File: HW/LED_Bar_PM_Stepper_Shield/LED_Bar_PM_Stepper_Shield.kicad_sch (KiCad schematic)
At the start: 14 parts, among them J5 1x6 2.54mm female, pin2 filled, J6 1x6 2.54mm female, pin2 filled, J7 Extension of Ard Nano, filled, J8 Extension of Ard Nano, filled

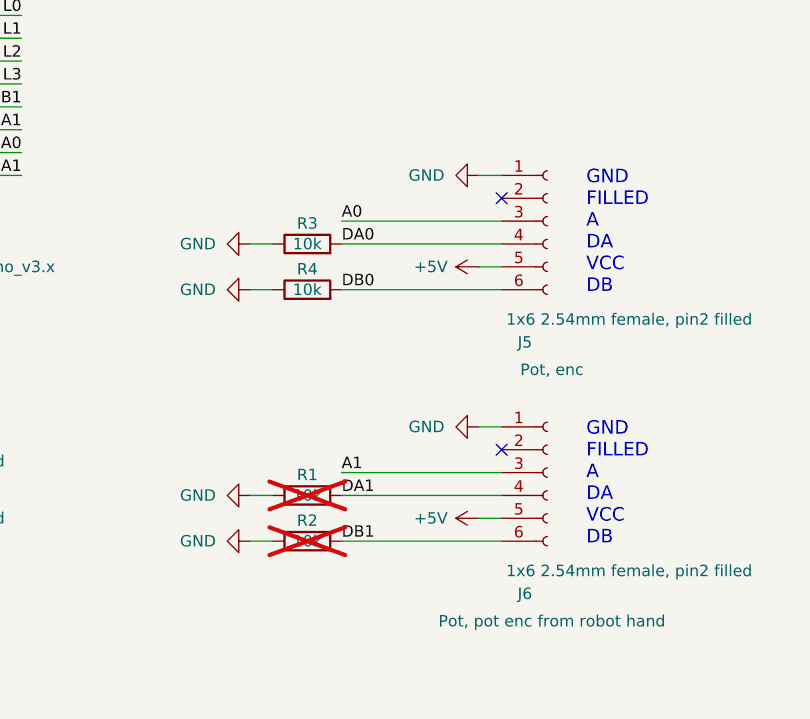
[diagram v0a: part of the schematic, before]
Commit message: Swapped GND and 5V so I can use internal Pull-up.
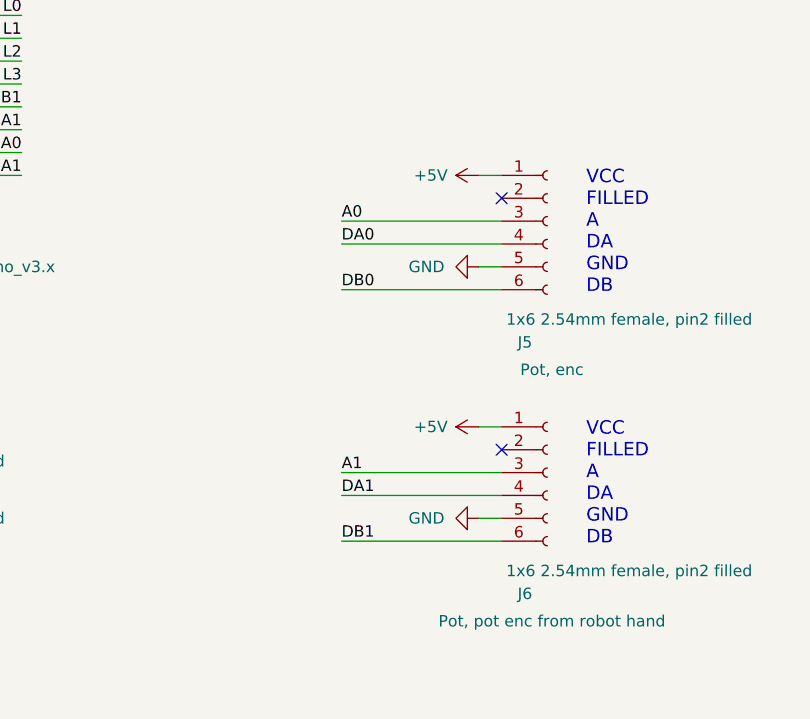
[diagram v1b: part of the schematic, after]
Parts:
- removed R1, R2, R3, R4: 10k, For_Rasterboard:R_Axial_DIN0207_L6.3mm_D2.5mm_Pinf_Horizontal, symbol Device:R
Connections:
- net +5V: now also J5.1 (Pin_1), J6.1 (Pin_1); no longer J5.5 (Pin_5), J6.5 (Pin_5)
- net GND: now also J5.5 (Pin_5), J6.5 (Pin_5); no longer J5.1 (Pin_1), J6.1 (Pin_1)
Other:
- note added: "VCC FILLED A DA GND DB"
- note removed: "GND FILLED A DA VCC DB"

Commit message: All done.
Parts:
- added D3, D5: 1N5400, Diode_THT:D_DO-201AD_P5.08mm_Vertical_AnodeUp, symbol Diode:1N5400
- added D4: 3mm yellow, For_Rasterboard:LED_D3.0mm_Pinf, symbol Device:LED
- added J10: 2-pin KK254, Connector_Molex:Molex_KK-254_AE-6410-02A_1x02_P2.54mm_Vertical, symbol Connector_Generic:Conn_01x02
- added J9: Barrel_Jack_Switch, Connector_BarrelJack:BarrelJack_Horizontal, symbol Connector:Barrel_Jack_Switch
- added Q1: IRLZ34N, Package_TO_SOT_THT:TO-220-3_Vertical, symbol Transistor_FET:IRLZ34N
- added R1: 470, For_Rasterboard:R_Axial_DIN0207_L6.3mm_D2.5mm_P7.62mm_Horizontal, symbol Device:R
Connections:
- net +5V: now also D3.1 (K), D4.2 (A), D5.1 (K), J10.1 (Pin_1), J9.1
- net GND: now also D5.2 (A), J9.2, J9.3, Q1.3 (S)
- net b0/B2 renamed S2
- net b0/B3 renamed S3
- net S3: now also Q1.1 (G)
- new net: D3.2 (A), J10.2 (Pin_2), Q1.2 (D), R1.2
- new net: D4.1 (K), R1.1
